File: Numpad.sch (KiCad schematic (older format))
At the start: 0 parts

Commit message: Schematic completed first draft
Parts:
- added C? (x3): 1n, symbol Device:C
- added U? (x3): 74LS597, symbol 74xx_IEEE:74LS597
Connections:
- new net: U?.14 (SER), U?.9 (QH) (x2)
- new net EXT1: U?.1 (B)
- new net EXT2: U?.2 (C)
- new net EXT3: U?.3 (D)
- new net EXT4: U?.4 (E)
- new net EXT5: U?.5 (F)
- new net EXT6: U?.6 (G)
- new net EXT7: U?.7 (H)
- new net GND: C?.2, C?.2, C?.2, U?.13 (~SLoad), U?.13 (~SLoad), U?.13 (~SLoad), U?.14 (SER), U?.8 (GND), U?.8 (GND), U?.8 (GND)
- new net NUM*: U?.2 (C)
- new net NUM+: U?.7 (H)
- new net NUM-: U?.3 (D)
- new net NUM.: U?.15 (A)
- new net NUM0: U?.7 (H)
- new net NUM1: U?.3 (D)
- new net NUM2: U?.4 (E)
- new net NUM3: U?.5 (F)
- new net NUM4: U?.15 (A)
- new net NUM5: U?.1 (B)
- new net NUM6: U?.2 (C)
- new net NUM7: U?.4 (E)
- new net NUM8: U?.5 (F)
- new net NUM9: U?.6 (G)
- new net NUME: U?.6 (G)
- new net NUML: U?.15 (A)
- new net NUMS: U?.1 (B)
- new net RESET: U?.10 (~R), U?.10 (~R), U?.10 (~R)
- new net SHIFT_0_DATA: U?.9 (QH)
- new net SHIFT_CLK: U?.11 (SCK), U?.11 (SCK), U?.11 (SCK)
- new net SHIFT_RCLK: U?.12 (CLK), U?.12 (CLK), U?.12 (CLK)
- new net VCC: C?.1, C?.1, C?.1, U?.16 (VCC), U?.16 (VCC), U?.16 (VCC)

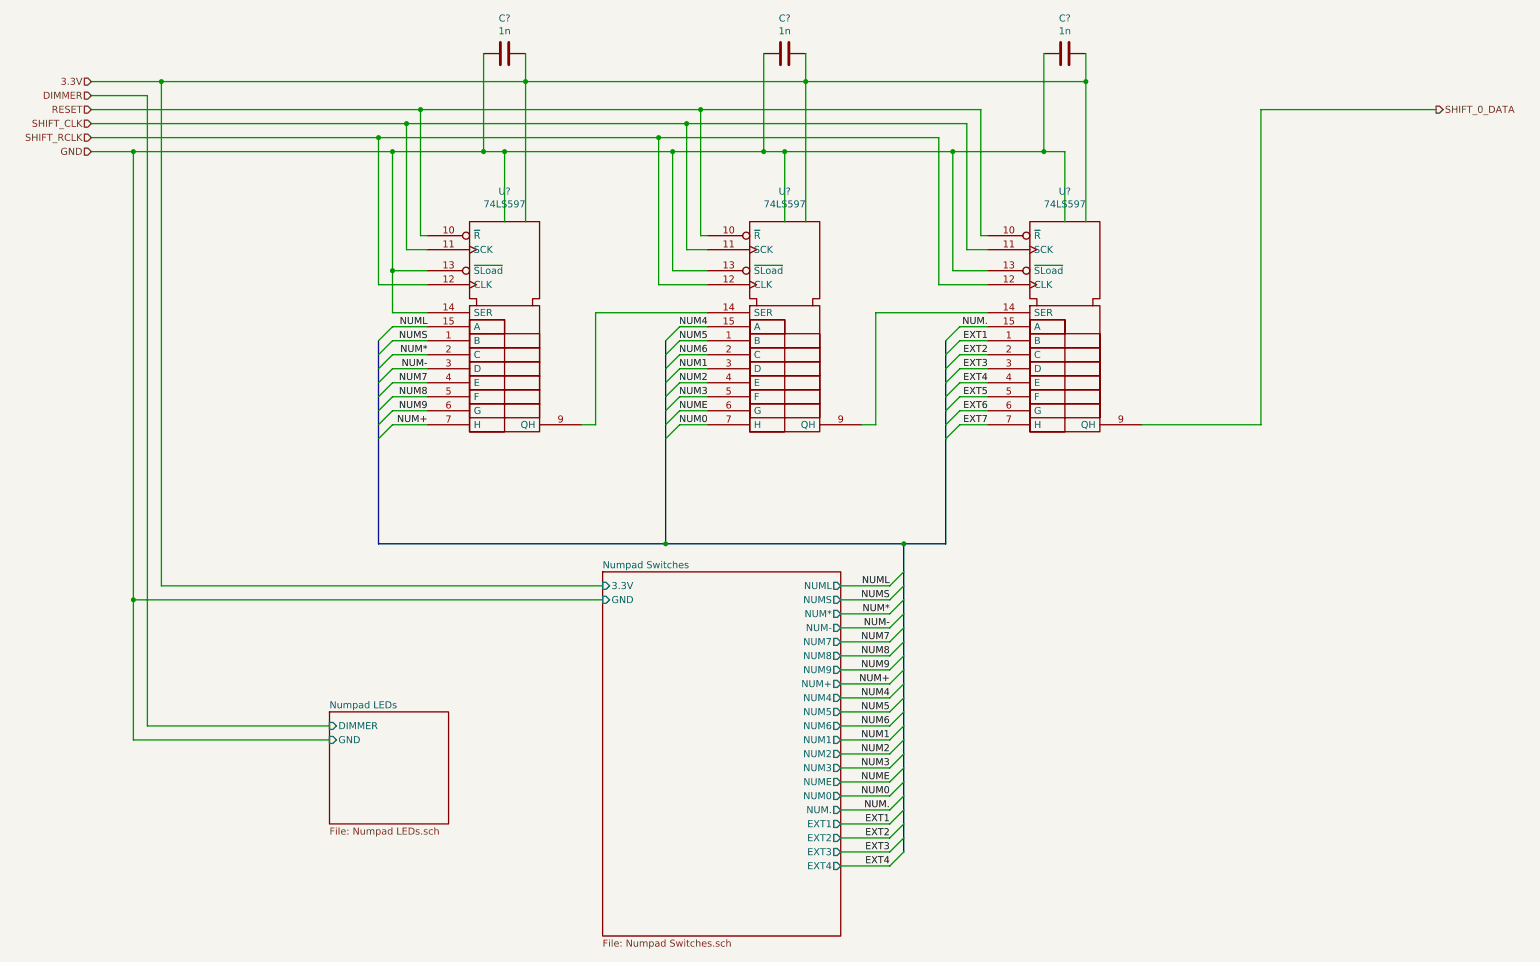
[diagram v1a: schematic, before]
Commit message: Fixed PISO Shift Register Wiring
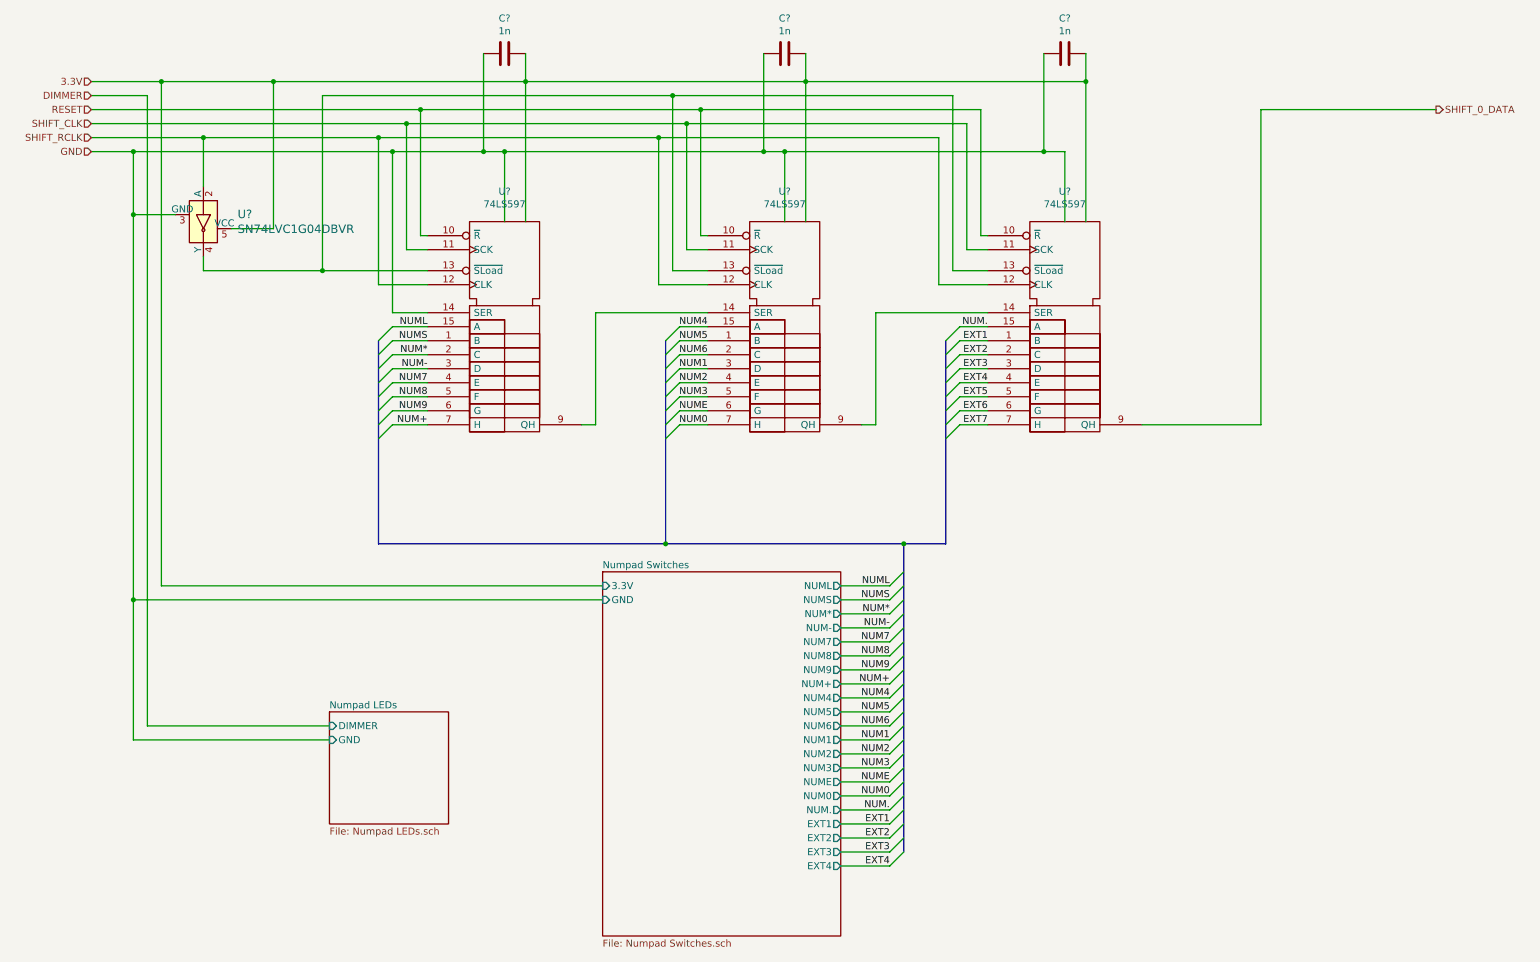
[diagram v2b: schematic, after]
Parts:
- added U?: SN74LVC1G04DBVR, digikey-footprints:SOT-753, symbol dk_Logic-Gates-and-Inverters:SN74LVC1G04DBVR
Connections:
- net GND: now also U?.3 (GND); no longer U?.13 (~SLoad), U?.13 (~SLoad), U?.13 (~SLoad)
- net SHIFT_RCLK: now also U?.2 (A)
- net VCC: now also U?.5 (VCC)
- new net: U?.13 (~SLoad), U?.13 (~SLoad), U?.13 (~SLoad), U?.4 (Y)
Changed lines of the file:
@@
 $Descr A4 11693 8268
 encoding utf-8
-Sheet 12 18
+Sheet 13 18
 Title ""
 Date ""
@@
 	3950 1600 3950 2100
 Wire Wire Line
-	3950 1600 5150 1600
-Wire Wire Line
 	5950 1600 5950 2100
 Connection ~ 3950 1600
@@
 Connection ~ 8100 1100
 Wire Wire Line
-	5950 1600 7150 1600
-Wire Wire Line
 	3350 1300 3350 2200
 Wire Wire Line
@@
 	7250 2300 7400 2300
 Connection ~ 5250 1400
-Wire Wire Line
-	3400 2450 3150 2450
-Wire Wire Line
-	3150 2450 3150 1600
 Connection ~ 3150 1600
 Wire Wire Line
@@
 	5400 2450 5150 2450
 Wire Wire Line
-	5150 2450 5150 1600
-Connection ~ 5150 1600
-Wire Wire Line
-	5150 1600 5800 1600
-Wire Wire Line
 	7400 2450 7150 2450
-Wire Wire Line
-	7150 2450 7150 1600
-Connection ~ 7150 1600
-Wire Wire Line
-	7150 1600 7800 1600
 Wire Wire Line
 	3050 1500 5050 1500
@@
 	5050 1500 7050 1500
 Wire Wire Line
-	3150 2450 3150 2750
-Wire Wire Line
 	3150 2750 3400 2750
-Connection ~ 3150 2450
 $Comp
 L Device:C C?
@@
 	9350 1300 9350 3550
 Wire Wire Line
-	1500 1100 4100 1100
+	1500 1100 2300 1100
 Connection ~ 1500 1100
 Wire Wire Line
@@
 	1000 1400 3250 1400
 Wire Wire Line
-	1000 1500 3050 1500
+	1000 1500 1800 1500
 Wire Wire Line
 	1300 1600 3150 1600
@@
 	8500 3550 9350 3550
 Wire Wire Line
-	1300 1600 1300 4800
+	1300 1600 1300 2050
 Wire Wire Line
 	4650 4800 1300 4800
@@
 Wire Bus Line
 	6800 4400 7100 4400
-Wire Bus Line
-	7100 2950 7100 4400
-Wire Bus Line
-	5100 2950 5100 4400
-Wire Bus Line
-	3050 2950 3050 4400
-Wire Bus Line
-	6800 4400 6800 6600
 Connection ~ 6800 4400
 $Sheet
@@
 F3 "GND" I L 2700 5800 50
 $EndSheet
+$Comp
+L dk_Logic-Gates-and-Inverters:SN74LVC1G04DBVR U?
+U 1 1 5EDA695B
+P 1800 2150
+AR Path="/5E8C755A/5EDA695B" Ref="U?"  Part="1"
+AR Path="/5E8C8F52/5EDA695B" Ref="U?"  Part="1"
+F 0 "U?" V 1697 2394 60  0000 L CNN
+F 1 "SN74LVC1G04DBVR" V 1803 2394 60  0000 L CNN
+F 2 "digikey-footprints:SOT-753" H 2000 2350 60  0001 L CNN
+F 3 "http://www.ti.com/general/docs/suppproductinfo.tsp?distId=10&gotoUrl=http%3A%2F%2Fwww.ti.com%2Flit%2Fgpn%2Fsn74lvc1g04" H 2000 2450 60  0001 L CNN
+F 4 "296-11599-1-ND" H 2000 2550 60  0001 L CNN "Digi-Key_PN"
+F 5 "SN74LVC1G04DBVR" H 2000 2650 60  0001 L CNN "MPN"
+F 6 "Integrated Circuits (ICs)" H 2000 2750 60  0001 L CNN "Category"
+F 7 "Logic - Gates and Inverters" H 2000 2850 60  0001 L CNN "Family"
+F 8 "http://www.ti.com/general/docs/suppproductinfo.tsp?distId=10&gotoUrl=http%3A%2F%2Fwww.ti.com%2Flit%2Fgpn%2Fsn74lvc1g04" H 2000 2950 60  0001 L CNN "DK_Datasheet_Link"
+F 9 "/product-detail/en/texas-instruments/SN74LVC1G04DBVR/296-11599-1-ND/385738" H 2000 3050 60  0001 L CNN "DK_Detail_Page"
+F 10 "IC INVERTER 1CH 1-INP SOT23-5" H 2000 3150 60  0001 L CNN "Description"
+F 11 "Texas Instruments" H 2000 3250 60  0001 L CNN "Manufacturer"
+F 12 "Active" H 2000 3350 60  0001 L CNN "Status"
+	1    1800 2150
+	0    1    1    0
+$EndComp
+Wire Wire Line
+	1600 2050 1300 2050
+Connection ~ 1300 2050
+Wire Wire Line
+	1300 2050 1300 4800
+Wire Wire Line
+	1800 1850 1800 1500
+Connection ~ 1800 1500
+Wire Wire Line
+	1800 1500 3050 1500
+Wire Wire Line
+	2000 2150 2300 2150
+Wire Wire Line
+	2300 2150 2300 1100
+Connection ~ 2300 1100
+Wire Wire Line
+	2300 1100 4100 1100
+Wire Wire Line
+	3150 1600 3150 2750
+Wire Wire Line
+	1800 2350 1800 2450
+Wire Wire Line
+	1800 2450 2650 2450
+Wire Wire Line
+	2650 2450 2650 1200
+Wire Wire Line
+	2650 1200 5150 1200
+Connection ~ 2650 2450
+Wire Wire Line
+	2650 2450 3400 2450
+Wire Wire Line
+	3950 1600 5800 1600
+Wire Wire Line
+	5950 1600 7800 1600
+Wire Wire Line
+	5150 1200 5150 2450
+Wire Wire Line
+	5150 1200 7150 1200
+Wire Wire Line
+	7150 1200 7150 2450
+Connection ~ 5150 1200
+Wire Bus Line
+	7100 2950 7100 4400
+Wire Bus Line
+	5100 2950 5100 4400
+Wire Bus Line
+	3050 2950 3050 4400
+Wire Bus Line
+	6800 4400 6800 6600
 $EndSCHEMATC

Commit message: Corrected errors found in design rule check
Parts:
- C88, C89, C90: renamed from C?; footprint (none) -> Capacitor_SMD:C_1206_3216Metric_Pad1.42x1.75mm_HandSolder
- U17, U18, U19: renamed from U?; footprint (none) -> Package_SO:SOIC-16_3.9x9.9mm_P1.27mm
- gave numbers to parts that had none: 1
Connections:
- net EXT5: no longer names the net of U19.5 (F)
- net EXT6: no longer names the net of U19.6 (G)
- net EXT7: no longer names the net of U19.7 (H)
- no-connect marks 0 -> 3
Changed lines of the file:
@@
 AR Path="/5E8C77AE/5E95E690" Ref="U?"  Part="1"
 AR Path="/5E8C755A/5E95E690" Ref="U?"  Part="1"
-AR Path="/5E8C8F52/5E95E690" Ref="U?"  Part="1"
-F 0 "U?" H 3950 3916 50  0000 C CNN
+AR Path="/5E8C8F52/5E95E690" Ref="U17"  Part="1"
+F 0 "U17" H 3950 3916 50  0000 C CNN
 F 1 "74LS597" H 3950 3825 50  0000 C CNN
-F 2 "" H 3950 2900 50  0001 C CNN
+F 2 "Package_SO:SOIC-16_3.9x9.9mm_P1.27mm" H 3950 2900 50  0001 C CNN
 F 3 "" H 3950 2900 50  0001 C CNN
 	1    3950 2900
@@
 AR Path="/5E8C77AE/5E95E696" Ref="U?"  Part="1"
 AR Path="/5E8C755A/5E95E696" Ref="U?"  Part="1"
-AR Path="/5E8C8F52/5E95E696" Ref="U?"  Part="1"
-F 0 "U?" H 5950 3916 50  0000 C CNN
+AR Path="/5E8C8F52/5E95E696" Ref="U18"  Part="1"
+F 0 "U18" H 5950 3916 50  0000 C CNN
 F 1 "74LS597" H 5950 3825 50  0000 C CNN
-F 2 "" H 5950 2900 50  0001 C CNN
+F 2 "Package_SO:SOIC-16_3.9x9.9mm_P1.27mm" H 5950 2900 50  0001 C CNN
 F 3 "" H 5950 2900 50  0001 C CNN
 	1    5950 2900
@@
 AR Path="/5E8C77AE/5E95E69C" Ref="U?"  Part="1"
 AR Path="/5E8C755A/5E95E69C" Ref="U?"  Part="1"
-AR Path="/5E8C8F52/5E95E69C" Ref="U?"  Part="1"
-F 0 "U?" H 7950 3916 50  0000 C CNN
+AR Path="/5E8C8F52/5E95E69C" Ref="U19"  Part="1"
+F 0 "U19" H 7950 3916 50  0000 C CNN
 F 1 "74LS597" H 7950 3825 50  0000 C CNN
-F 2 "" H 7950 2900 50  0001 C CNN
+F 2 "Package_SO:SOIC-16_3.9x9.9mm_P1.27mm" H 7950 2900 50  0001 C CNN
 F 3 "" H 7950 2900 50  0001 C CNN
 	1    7950 2900
@@
 AR Path="/5E8C77AE/5E95E6E4" Ref="C?"  Part="1"
 AR Path="/5E8C755A/5E95E6E4" Ref="C?"  Part="1"
-AR Path="/5E8C8F52/5E95E6E4" Ref="C?"  Part="1"
-F 0 "C?" V 3698 900 50  0000 C CNN
+AR Path="/5E8C8F52/5E95E6E4" Ref="C88"  Part="1"
+F 0 "C88" V 3698 900 50  0000 C CNN
 F 1 "1n" V 3789 900 50  0000 C CNN
-F 2 "" H 3988 750 50  0001 C CNN
+F 2 "Capacitor_SMD:C_1206_3216Metric_Pad1.42x1.75mm_HandSolder" H 3988 750 50  0001 C CNN
 F 3 "~" H 3950 900 50  0001 C CNN
 	1    3950 900
@@
 AR Path="/5E8C77AE/5E95E6EA" Ref="C?"  Part="1"
 AR Path="/5E8C755A/5E95E6EA" Ref="C?"  Part="1"
-AR Path="/5E8C8F52/5E95E6EA" Ref="C?"  Part="1"
-F 0 "C?" V 5698 900 50  0000 C CNN
+AR Path="/5E8C8F52/5E95E6EA" Ref="C89"  Part="1"
+F 0 "C89" V 5698 900 50  0000 C CNN
 F 1 "1n" V 5789 900 50  0000 C CNN
-F 2 "" H 5988 750 50  0001 C CNN
+F 2 "Capacitor_SMD:C_1206_3216Metric_Pad1.42x1.75mm_HandSolder" H 5988 750 50  0001 C CNN
 F 3 "~" H 5950 900 50  0001 C CNN
 	1    5950 900
@@
 AR Path="/5E8C77AE/5E95E6F0" Ref="C?"  Part="1"
 AR Path="/5E8C755A/5E95E6F0" Ref="C?"  Part="1"
-AR Path="/5E8C8F52/5E95E6F0" Ref="C?"  Part="1"
-F 0 "C?" V 7698 900 50  0000 C CNN
+AR Path="/5E8C8F52/5E95E6F0" Ref="C90"  Part="1"
+F 0 "C90" V 7698 900 50  0000 C CNN
 F 1 "1n" V 7789 900 50  0000 C CNN
-F 2 "" H 7988 750 50  0001 C CNN
+F 2 "Capacitor_SMD:C_1206_3216Metric_Pad1.42x1.75mm_HandSolder" H 7988 750 50  0001 C CNN
 F 3 "~" H 7950 900 50  0001 C CNN
 	1    7950 900
@@
 Wire Wire Line
 	7400 3250 7200 3250
-Wire Wire Line
-	7400 3350 7200 3350
-Wire Wire Line
-	7400 3450 7200 3450
-Wire Wire Line
-	7400 3550 7200 3550
 Text Label 7400 3250 2    50   ~ 0
 EXT4
-Text Label 7400 3350 2    50   ~ 0
-EXT5
-Text Label 7400 3450 2    50   ~ 0
-EXT6
-Text Label 7400 3550 2    50   ~ 0
-EXT7
 Wire Wire Line
 	3150 2850 3400 2850
@@
 	3150 3550 3400 3550
 Entry Wire Line
-	7100 3450 7200 3350
-Entry Wire Line
 	7100 3350 7200 3250
-Entry Wire Line
-	7100 3550 7200 3450
-Entry Wire Line
-	7100 3650 7200 3550
 $Sheet
 S 4650 4600 1700 2600
@@
 P 1800 2150
 AR Path="/5E8C755A/5EDA695B" Ref="U?"  Part="1"
-AR Path="/5E8C8F52/5EDA695B" Ref="U?"  Part="1"
-F 0 "U?" V 1697 2394 60  0000 L CNN
+AR Path="/5E8C8F52/5EDA695B" Ref="U16"  Part="1"
+F 0 "U16" V 1697 2394 60  0000 L CNN
 F 1 "SN74LVC1G04DBVR" V 1803 2394 60  0000 L CNN
 F 2 "digikey-footprints:SOT-753" H 2000 2350 60  0001 L CNN
@@
 	7150 1200 7150 2450
 Connection ~ 5150 1200
+NoConn ~ 7400 3350
+NoConn ~ 7400 3450
+NoConn ~ 7400 3550
 Wire Bus Line
 	7100 2950 7100 4400
